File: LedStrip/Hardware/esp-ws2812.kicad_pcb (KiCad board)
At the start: 2 copper layers, 28 x 12 mm, 13 parts, among them P1 CONN_01X02, P3 CONN_01X01, P4 CONN_01X02, Q1 BSS138, U1 MCP1700, U2 ESP-01v090

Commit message: board update
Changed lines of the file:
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@@
     (35 F.Paste user)
     (36 B.SilkS user)
-    (37 F.SilkS user)
+    (37 F.SilkS user hide)
     (38 B.Mask user)
     (39 F.Mask user)
@@
     (descr "Through hole pin header")
     (tags "pin header")
-    (fp_text reference P3 (at 6.8 -2.4) (layer B.SilkS)
-      (effects (font (size 1 1) (thickness 0.15)) (justify mirror))
+    (fp_text reference P3 (at 7 -1.8 180) (layer B.SilkS)
+      (effects (font (size 0.8 0.8) (thickness 0.15)) (justify mirror))
     )
     (fp_text value CONN_01X01 (at 5 0.15 90) (layer F.Fab)
@@
     (tags "resistor 0805")
     (attr smd)
-    (fp_text reference R2 (at 1.4 -2.05 270) (layer F.SilkS)
+    (fp_text reference R2 (at 0.4 1.75 270) (layer F.SilkS)
       (effects (font (size 1 1) (thickness 0.15)))
     )
@@
     (descr "Through hole pin header")
     (tags "pin header")
-    (fp_text reference P4 (at -2.4 2.94 360) (layer B.SilkS)
-      (effects (font (size 1 1) (thickness 0.15)) (justify mirror))
+    (fp_text reference P4 (at -1.8 3.54 180) (layer B.SilkS)
+      (effects (font (size 0.8 0.8) (thickness 0.15)) (justify mirror))
     )
     (fp_text value CONN_01X02 (at 5 -3.45 180) (layer F.Fab)
@@
     (descr "Radial Electrolytic Capacitor, Diameter 6.3mm x Length 11.2mm, Pitch 2.5mm")
     (tags "Electrolytic Capacitor")
-    (fp_text reference C5 (at 0.2 1.6 270) (layer B.SilkS)
-      (effects (font (size 1 1) (thickness 0.15)) (justify mirror))
+    (fp_text reference C5 (at 1.4 -1.6 450) (layer B.SilkS)
+      (effects (font (size 0.8 0.8) (thickness 0.15)) (justify mirror))
     )
     (fp_text value 1000uf (at 1.25 4.4 270) (layer F.Fab)

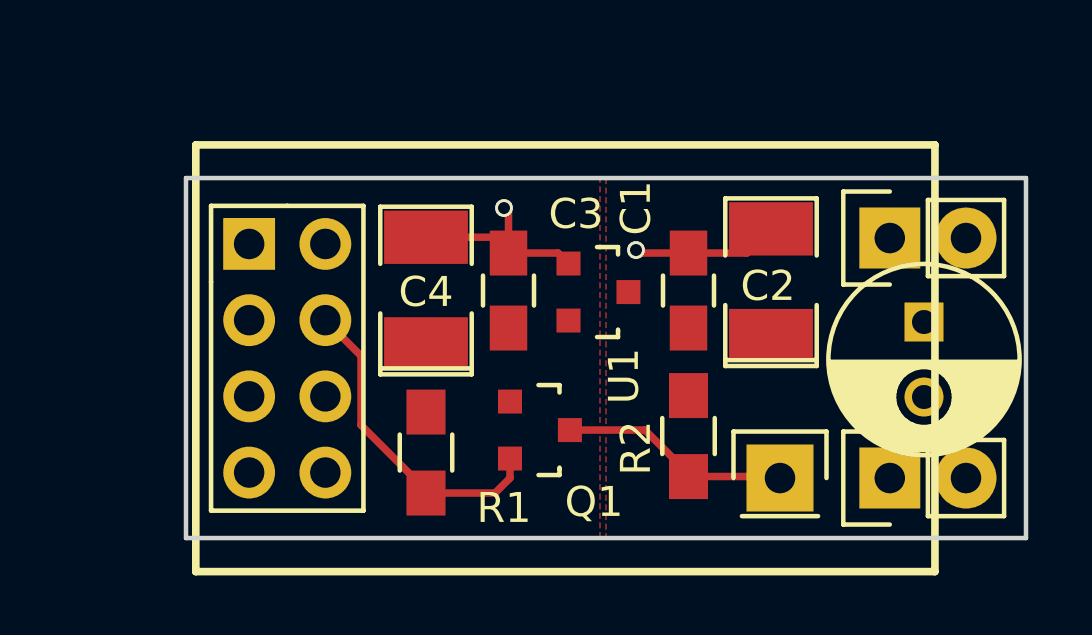
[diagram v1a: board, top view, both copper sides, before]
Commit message: added a uart/gpio0 interface to the esp board
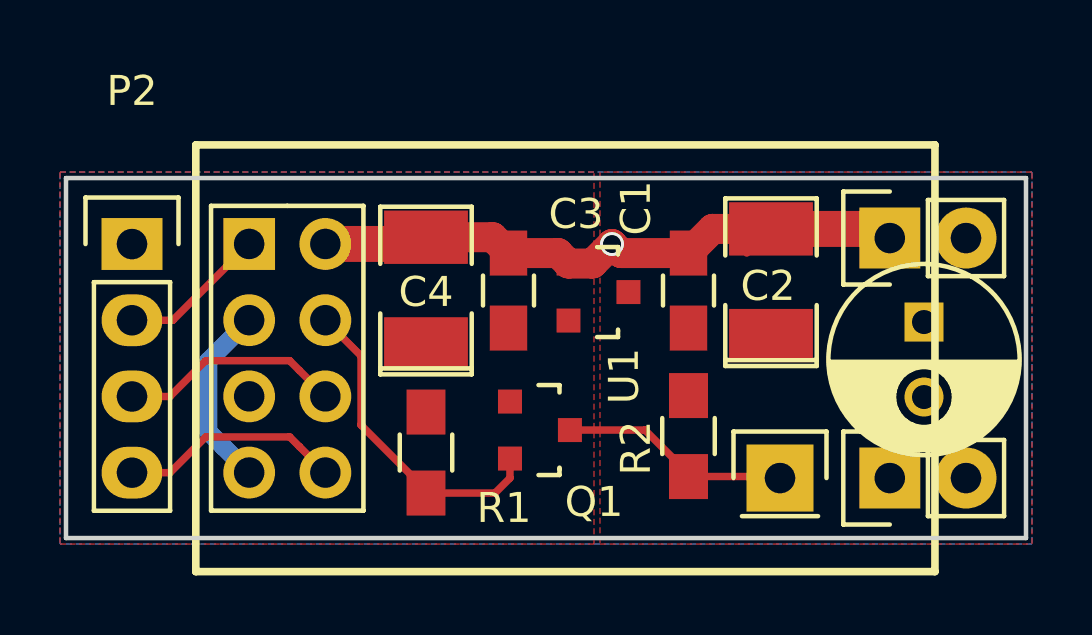
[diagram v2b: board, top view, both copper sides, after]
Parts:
- added P2: CONN_01X04, Pin_Headers:Pin_Header_Straight_1x04, F.Cu at (148.2, 92.2)
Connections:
- U2 pad 1: (no net) -> TX
- U2 pad 6: (no net) -> GPIO0
- U2 pad 8: (no net) -> RX
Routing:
- net GND: track 11.6 -> 21.3 mm, vias 2 -> 1
- net GPIO0: track 0.00 -> 7.43 mm
- net RX: track 0.00 -> 7.43 mm
- net +3V3: track 0.00 -> 6.21 mm
- net TX: track 0.00 -> 4.96 mm
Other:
- board size 28 x 12 mm -> 32 x 12 mm
- board text added: "G0"
- board text added: "GND"
- board text added: "RX"
- board text added: "TX"
